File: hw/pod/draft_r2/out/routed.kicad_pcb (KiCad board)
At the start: 4 copper layers, 30 x 12 mm, 74 parts, among them J1 XDCR_A, J10 D+, J11 D-, J12 CC, J2 XDCR_B, J3 VBUS, J4 GND, J5 BAT+, J7 LED+, J8 LED-, J9 NTC, Q1 PMCXB290UE, Q2 PMCXB290UE, SW1 KMT022NGJLHS, U1 STM32U575CIUxQ, U2 SPH0641LU4H-1, U3 BQ25180YBGR, U4 TPS7A2030PDQNR, U6 TPD2E2U06DRLR, Y1 32.768k 7pF

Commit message: Board: redundant +3V0 via removed (hole-to-hole 0.109 mm) - DRC now 0 violations, 0 unconnected, parity 0; noise metrics identical
The two +3V0 vias (11.37, 1.28) / (11.595, 1.152) both joined the same B-side copper
(U1 pin 9 VDDA <-> C6 pad 1, linked on B) to the In2 plane. Deleted via d5fef857 and its
0.86 mm stub from U1.9 (pcbnew, authorised); kept the via at C6 pad 1, so the supply path
is plane -> via -> C6 -> pin 9 (decoupling cap before the pin).
DRC (kicad-cli, schematic parity): 0 violations, 0 unconnected, parity 0 (was 1 warning).
Noise smoke: LN-M01 26.5 dB, M02 20.1, M03 1.29 %, M04 0.1267 mV, M05 8.718 uV,
M06 0.1074 mV, identical; layout-noise.yaml sha 36d088d4 -> 21bbe68f, 595 segments /
129 vias; smoke exit 0. plm 0/0/0/0.

Co-Authored-By: Claude Opus 5.5 <noreply@anthropic.com>
Claude-Session: https://claude.ai/code/session_01Wg997D6KFs8bxoAH56jZZJ
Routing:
- net +3V0: track 17.7 -> 16.9 mm, vias 23 -> 22
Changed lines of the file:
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@@
-	)
-	(via
-		(at 11.5948 1.1519)
-		(size 0.35)
-		(drill 0.15)
-		(layers "F.Cu" "B.Cu")
-		(net "+3V0")
 	)
 	(via
@@
 		(width 0.15)
 		(layer "B.Cu")
-		(net "+3V0")
-	)
-	(segment
-		(start 11.3 1.9625)
-		(end 11.5948 1.1519)
-		(width 0.15)
-		(layer "B.Cu")

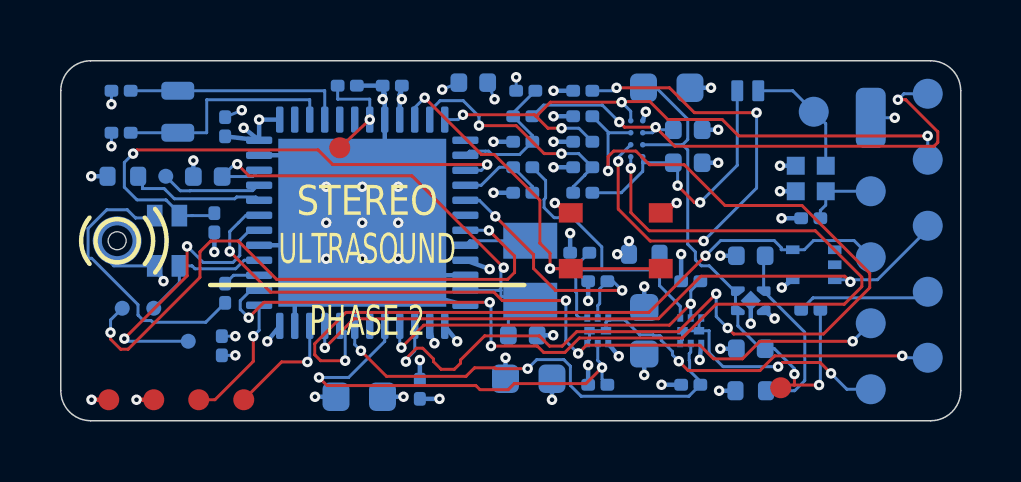
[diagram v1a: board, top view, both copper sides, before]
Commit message: Router batch (round 8): R23 1M I_SENSE offset (OUT-1B), TP2/TP4 swap (DBG-2), mic port D0.65 (SAI-15D) - local re-route, DRC 0/0/0 incl. warnings
Schematic (gen.py, Phase-2 only so the Rev G reference stays frozen): R23 1M 0201
(C473482, existing line) +3V0 -> I_SENSE. 100k was the first value but +3V0 stays up in
Off and 100k drew 29.7 uA (> the 16.5-24 uA Off budget); 1M = 3.0 uA, +3.0 mV offset;
selftest_lockin.py (now R_OFF env) at 1M: -12 dBFS |Z| 2.07 %, phase 0.89 deg (100k:
1.91 / 0.73), min ADC input 2.7 mV (no negative samples).
Mic: new footprint Knowles_LGA-5_3.5x2.65mm_Port0.65 (Port0.6 kept for Rev F): NPTH D0.65
at local (0, 0.75) -> board (1.90, 6.0); +0.02 so pad 3 clearance is 0.2075 (D0.65 at the
old spot: 0.1875 < 0.2). Order with JLC press-fit tolerance (0.60-0.70).
Placement: R23 (19.2, 5.15) B; TP2 SWCLK (3.1, 11.3) / TP4 +3V0 (4.6, 11.3).
Route: local_reroute.py (R23 + TPs moved; BTN, I_SENSE, SWCLK ripped and re-routed),
pruned the NRST pre-via, R23 fields on B.Fab like the rest.
DK-17D (R24 1k DOCK_VBUS -> PA9) did NOT route locally: 14 passes + hand escapes, U1's
bottom-row fan-out has no free lane once pin 30 is used; backed out (reg-board issue 22).
Checks: kicad-cli DRC (all severities, schematic parity): 0 violations / 0 unconnected /
parity 0; place_r2 check PASS; noise smoke PASS (LN-M01 26.5, M02 20.1 dB, M03 1.29 ->
1.32 %, M04 0.1267 -> 0.1269 mV, M05 8.718 -> 8.721 uV, M06 0.1074 -> 0.1076 mV);
acoustics MC60 phase2_r2: mean +5.58 -> +5.93 dB, MC p05/p50 -0.06/4.51 -> +1.22/5.20,
R14 all-pass 0.70 -> 0.63 (20-80 kHz 0.77 both), duct peak 63.0 kHz +18.48 -> 61.3 kHz
+18.44 dB; interfaces/bom_check no FAIL (phase2; revg only its pre-existing cost-bom);
shell_r2 valid (duct follows the hole: dims_r2 reads its offset; limit 0.175, pin 0.14).
Tooling: interfaces [mic-port] uses the gauge-pin residual as the stack when the board is
located; [rails] skips loads of parts a design does not have; dims_r2 MIC_HOLE_D 0.65,
press-fit hole tol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
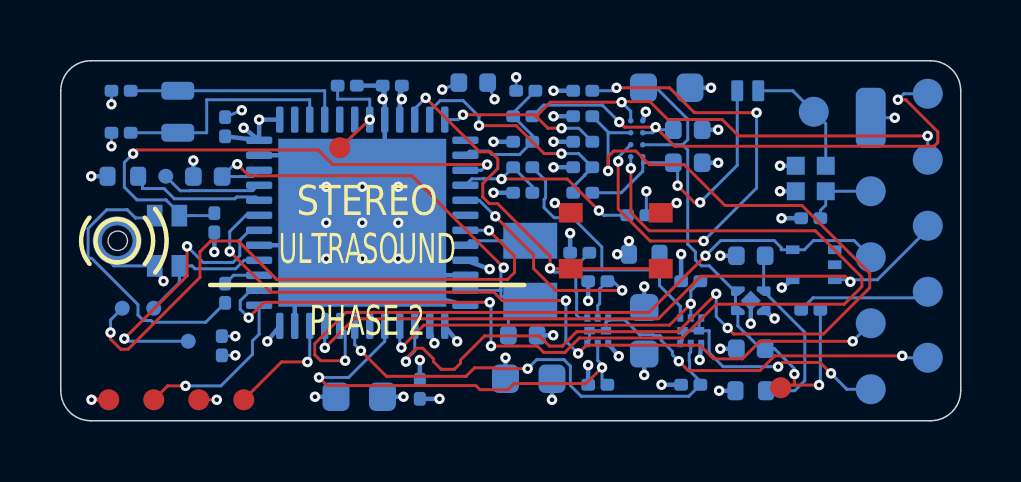
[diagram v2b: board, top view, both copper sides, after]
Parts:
- added R23: 1M, R_0201_0603Metric, B.Cu at (19.2, 5.15)
- U2: footprint Knowles_LGA-5_3.5x2.65mm_Port0.6 -> Knowles_LGA-5_3.5x2.65mm_Port0.65
- moved TP2 1.50 mm to (3.10, 11.3)
- moved TP4 1.50 mm to (4.60, 11.3)
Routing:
- net I_SENSE: track 2.96 -> 7.65 mm, vias 0 -> 2
- net SWCLK: track 4.30 -> 5.65 mm
- net +3V0: track 16.9 -> 17.7 mm, vias 22 -> 23
- net BTN: track 13.8 -> 14.4 mm
